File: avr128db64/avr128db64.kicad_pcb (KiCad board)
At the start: 2 copper layers, 99.8 x 49.9 mm, 38 parts, among them J1 BUS, J2 47571-0001, J3 UEXT, J4 SERIAL, Q1 FDG6335N, SW1 Reset, SW2 BANK ENA, SW3 SW_DIP_x06, U1 AVR128DB64x-xPT, U2 MIC5504-3.3YM5, U3 MCP7940N-xST, U5 74HCT574, U6 74HCT257, U7 AS6C4008-55PCN, Y1 32kHz

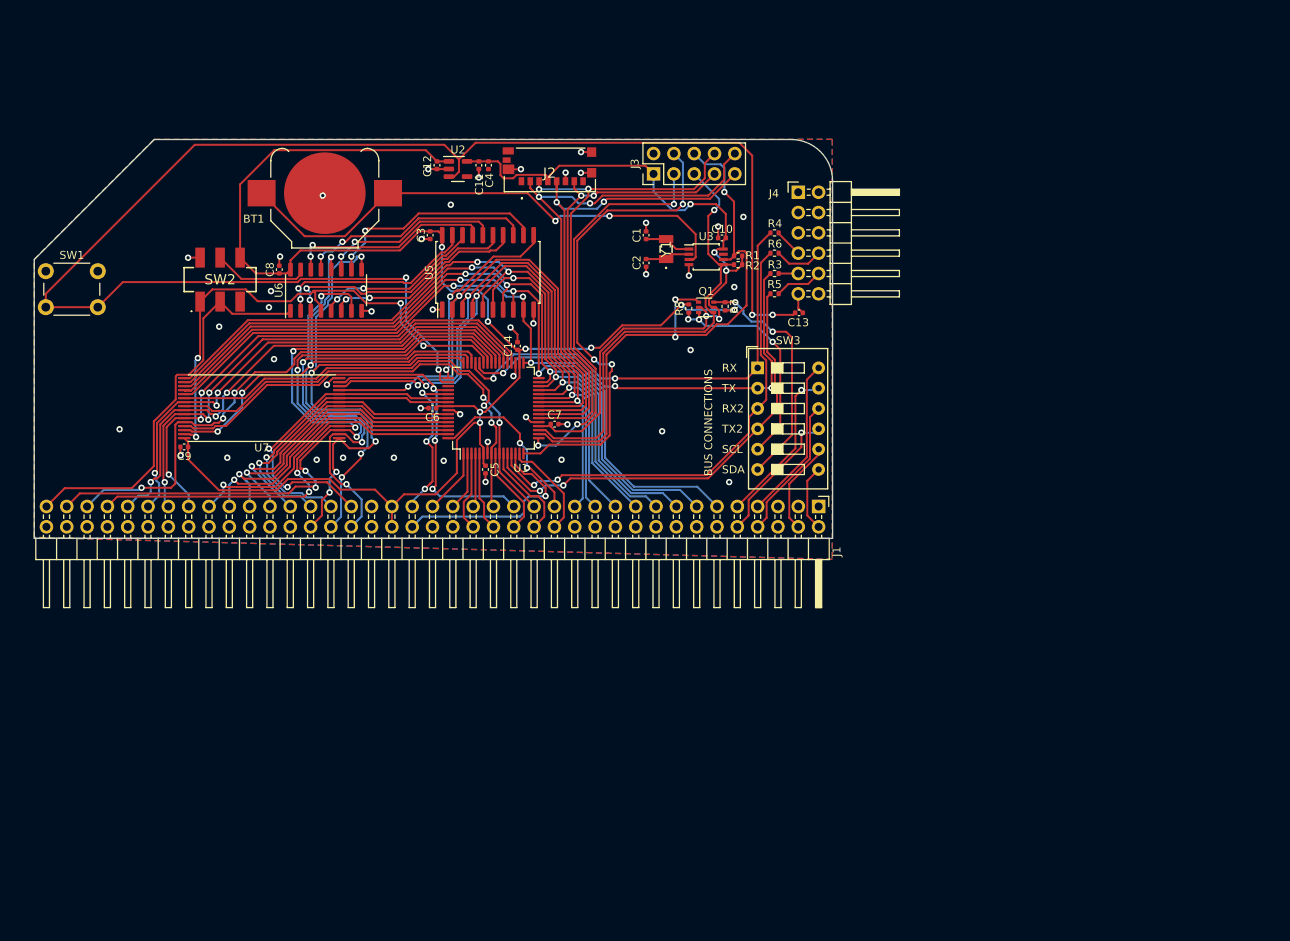
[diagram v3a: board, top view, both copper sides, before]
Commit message: Move to hybrid layout: TH RAM and Logic ICs
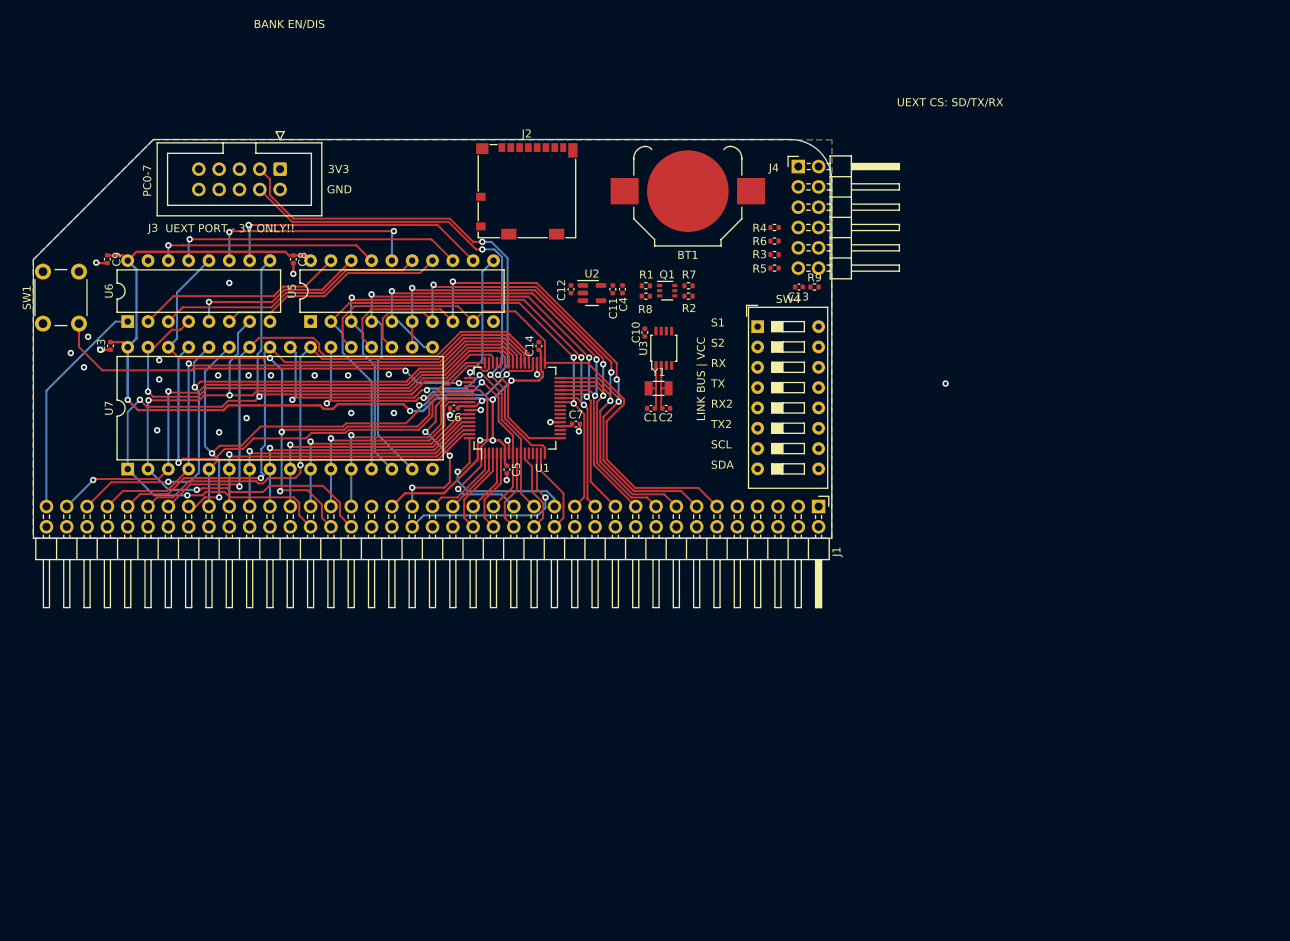
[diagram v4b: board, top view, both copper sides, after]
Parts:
- removed SW2: BANK ENA, SamacSys_Parts:JS202011SCQN
- removed SW3: SW_DIP_x06, Button_Switch_THT:SW_DIP_SPSTx06_Slide_9.78x17.42mm_W7.62mm_P2.54mm
- added R9: 1K, Resistor_SMD:R_0402_1005Metric, F.Cu at (190.2, 76.7)
- added SW4: SW_DIP_x08, Button_Switch_THT:SW_DIP_SPSTx08_Slide_9.78x22.5mm_W7.62mm_P2.54mm, F.Cu at (183.1, 81.7)
- J2: value 47571-0001 -> Micro_SD_Card_Det2; footprint SamacSys_Parts:475710001 -> Connector_Card:microSD_HC_Molex_104031-0811
- J3: footprint Connector_PinHeader_2.54mm:PinHeader_2x05_P2.54mm_Vertical -> Connector_IDC:IDC-Header_2x05_P2.54mm_Vertical
- SW1: value Reset -> RESET
- U5: footprint Package_SO:SOIC-20W_7.5x12.8mm_P1.27mm -> Package_DIP:DIP-20_W7.62mm
- U6: footprint Package_SO:SO-16_3.9x9.9mm_P1.27mm -> Package_DIP:DIP-16_W7.62mm
- U7: footprint Package_SO:TSOP-I-32_18.4x8mm_P0.5mm -> Package_DIP:DIP-32_W15.24mm
- Y1: footprint SamacSys_Parts:SC32S7PF20PPM -> Crystal:Crystal_SMD_3215-2Pin_3.2x1.5mm
- moved J3 46.7 mm to (123.4, 62.0), turned to -90 degrees
- moved BT1 45.4 mm to (174.4, 64.7)
- moved C3 42.3 mm to (102.2, 84.1)
- moved C9 25.4 mm to (101.9, 73.2), turned to -90 degrees
- moved U6 25.1 mm to (104.4, 81.0)
- moved U5 23.0 mm to (127.3, 81.0)
- moved C12 22.8 mm to (159.8, 77.0)
- moved C11 22.8 mm to (165.0, 77.0)
- moved C4 22.8 mm to (166.2, 77.0)
- moved U2 22.8 mm to (162.4, 77.5)
- moved C1 21.6 mm to (169.8, 91.9), turned to 180 degrees
- moved U7 18.4 mm to (104.4, 99.5), turned to 90 degrees
- moved C2 18.4 mm to (171.7, 91.9), turned to 0 degrees
- moved Y1 17.4 mm to (170.8, 89.4), turned to 0 degrees
- moved C10 15.3 mm to (169.0, 82.4), turned to -90 degrees
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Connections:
- net /~{CS1}/TX3 renamed /TX3
- net /~{CS2}/RX3 renamed /RX3
- net /~{RST} renamed /~{Z80RST}
- C13 pad 1: /AVRRST -> Net-(J4-Pin_11)
- C13 pad 2: Net-(J4-Pin_11) -> /~{RESET}
- J3 pad 10: /~{SDCS} -> Net-(J3-Pin_10)
- J4 pad 5: unconnected-(J4-Pin_5-Pad5) -> Net-(J4-Pin_5)
- J4 pad 6: unconnected-(J4-Pin_6-Pad6) -> Net-(J4-Pin_6)
- SW1 pad 2: /AVRRST -> /~{RESET}
- U1 pad 50: /AVRRST -> /~{RESET}
- U2 pad 3: /AVRRST -> /~{RESET}
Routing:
- net /AVRRST: track 190.7 -> 0.00 mm, vias 4 -> 0
- net +3.3V: track 95.9 -> 1.60 mm, vias 5 -> 0
- net /SDA: track 73.2 -> 0.00 mm, vias 3 -> 0
- net Net-(BT1-+): track 65.2 -> 0.00 mm, vias 2 -> 0
- net /~{SDCS}: track 64.6 -> 0.00 mm, vias 2 -> 0
- net /MOSI: track 62.8 -> 0.00 mm, vias 2 -> 0
- net /SCK: track 61.1 -> 0.00 mm, vias 2 -> 0
- net /RX2: track 59.1 -> 0.00 mm, vias 2 -> 0
- net /SCL: track 58.4 -> 0.00 mm, vias 1 -> 0
- net +5V: track 194.6 -> 136.6 mm, vias 8 -> 7
- net /RX: track 57.4 -> 0.00 mm, vias 2 -> 0
- net /TX2: track 56.0 -> 0.00 mm, vias 2 -> 0
- net /TX: track 55.0 -> 0.00 mm, vias 3 -> 0
- net /MISO: track 54.9 -> 0.00 mm, vias 2 -> 0
- net /~{RESET}: track 0.00 -> 53.9 mm, vias 0 -> 2
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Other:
- board text added: "3V3"
- board text added: "BANK EN/DIS"
- board text added: "GND"
- board text added: "LINK BUS | VCC"
- board text added: "PC0-7"
- board text added: "S1"
- board text added: "S2"
- board text added: "UEXT CS: SD/TX/RX"
- board text added: "UEXT PORT - 3V ONLY!!"
- board text added: "___ ___ _ _ ___( _ ) / _ \ ___| |_ _ __| | |_ / _ \| | | |/ __| __| '__| | / / (_) | |_| | (__| |_| | | | /___\___/ \___/ \___|\__|_| |_| z80ctrl DB REV1 (C)2023 J.B. Langston https://github.com/jblang/z80ctrl"
- board text removed: "BUS CONNECTIONS"

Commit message: Finish layout for hybrid design
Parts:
- added J5: Conn_01x04_Pin, Connector_PinHeader_2.54mm:PinHeader_1x04_P2.54mm_Horizontal, F.Cu at (191.0, 79.9)
- added SW2: SW_DPDT_x2, SamacSys_Parts:JS202011CQN, F.Cu at (96.2, 92.6)
- added SW3: SW_SP3T, SamacSys_Parts:OS103011MS8QP1, F.Cu at (138.2, 61.1)
- added SW5: SW_DPDT_x2, SamacSys_Parts:JS202011CQN, F.Cu at (189.3, 97.4)
- added SW6: SW_DPDT_x2, SamacSys_Parts:JS202011CQN, F.Cu at (171.5, 81.5)
- Q1: value FDG6335N -> BSS138
- SW4: value SW_DIP_x08 -> SW_DIP_x06; footprint Button_Switch_THT:SW_DIP_SPSTx08_Slide_9.78x22.5mm_W7.62mm_P2.54mm -> Button_Switch_THT:SW_DIP_SPSTx06_Slide_9.78x17.42mm_W7.62mm_P2.54mm
- moved R9 91.5 mm to (98.8, 72.7)
- moved SW4 22.8 mm to (170.5, 100.6), turned to 90 degrees
- moved C1 16.9 mm to (170.9, 75.0), turned to 90 degrees
- moved C4 16.1 mm to (161.7, 61.5)
- moved R8 15.7 mm to (183.5, 84.3)
- moved R1 15.7 mm to (183.5, 83.0), turned to 180 degrees
- moved C2 15.0 mm to (170.9, 76.9), turned to -90 degrees
- moved C10 13.7 mm to (180.1, 74.3), turned to 180 degrees
- moved Y1 13.7 mm to (173.4, 76.0), turned to -90 degrees
- moved Q1 11.1 mm to (180.8, 83.6)
- moved U3 10.5 mm to (178.4, 76.6), turned to 0 degrees
- moved R2 7.41 mm to (178.2, 84.3), turned to 0 degrees
- moved R7 7.41 mm to (178.2, 83.0)
- moved C13 2.45 mm to (190.8, 76.7)
- moved C11 1.26 mm to (166.1, 76.3)
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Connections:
- Q1 pad 1: /SDA -> /SDA3V
- Q1 pad 4: /SCL -> /SCL3V
- R1 pad 1: +3.3V -> +5V
- R1 pad 2: /SDA -> /SDA5V
- R2 pad 1: +3.3V -> +5V
- R2 pad 2: /SCL -> /SCL5V
- R7 pad 1: /SDA5V -> +3.3V
- R7 pad 2: +5V -> /SDA3V
- R8 pad 1: /SCL5V -> +3.3V
- R8 pad 2: +5V -> /SCL3V
- SW4 pad 1: Net-(J4-Pin_6) -> +5V
- SW4 pad 10: /USER6 -> /RX
- SW4 pad 11: /BTX2 -> Net-(J4-Pin_5)
- SW4 pad 12: /BRX2 -> Net-(J4-Pin_6)
- SW4 pad 2: Net-(J4-Pin_5) -> +5V
- SW4 pad 3: /RX -> /BRX
- SW4 pad 4: /TX -> /BTX
- SW4 pad 5: /RX2 -> /BRX2
- SW4 pad 6: /TX2 -> /BTX2
- SW4 pad 7: /SCL5V -> /TX2
- SW4 pad 8: /SDA5V -> /RX2
- SW4 pad 9: /USER7 -> /TX
- U3 pad 5: /SCL -> /SDA3V
- U3 pad 6: /SDA -> /SCL3V
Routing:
- net +3.3V: track 1.60 -> 129.9 mm, vias 0 -> 7
- net GND: track 12.5 -> 128.8 mm, vias 27 -> 34
- net /~{RESET}: track 53.9 -> 147.7 mm, vias 2 -> 8
- net +5V: track 136.6 -> 226.5 mm, vias 7 -> 12
- net /SCL: track 0.00 -> 88.9 mm, vias 0 -> 3
- net /SDA: track 0.00 -> 85.9 mm, vias 0 -> 3
- net /RX: track 0.00 -> 67.4 mm, vias 0 -> 1
- net /RX2: track 0.00 -> 66.3 mm, vias 0 -> 3
- net /TX: track 0.00 -> 63.5 mm, vias 0 -> 1
- net /~{SDCS}: track 0.00 -> 60.9 mm, vias 0 -> 3
- net /TX2: track 0.00 -> 54.3 mm, vias 0 -> 3
- net Net-(J4-Pin_6): track 0.00 -> 46.8 mm
- net /MOSI: track 0.00 -> 44.5 mm, vias 0 -> 2
- net /MISO: track 0.00 -> 43.8 mm, vias 0 -> 2
- net /SCK: track 0.00 -> 40.8 mm, vias 0 -> 2
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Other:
- board text added: "BANK ON/OFF"
- board text added: "I2C 5V"
- board text added: "I2C ENABLE"
- board text added: "RESET"
- board text added: "SERIAL LINK"
- board text added: "UEXT CS: SD/RX/TX"
- board text added: "UPDI"
- board text added: "VCC1"
- board text added: "VCC2"
- board text removed: "3V3"
- board text removed: "GND"
- board text removed: "LINK BUS | VCC"
- board text removed: "PC0-7"
- board text removed: "S1"
- board text removed: "S2"
- board text removed: "SCL"
- board text removed: "SDA"
